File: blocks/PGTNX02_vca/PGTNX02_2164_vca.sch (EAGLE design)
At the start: 72 parts, among them IC3 TL074P

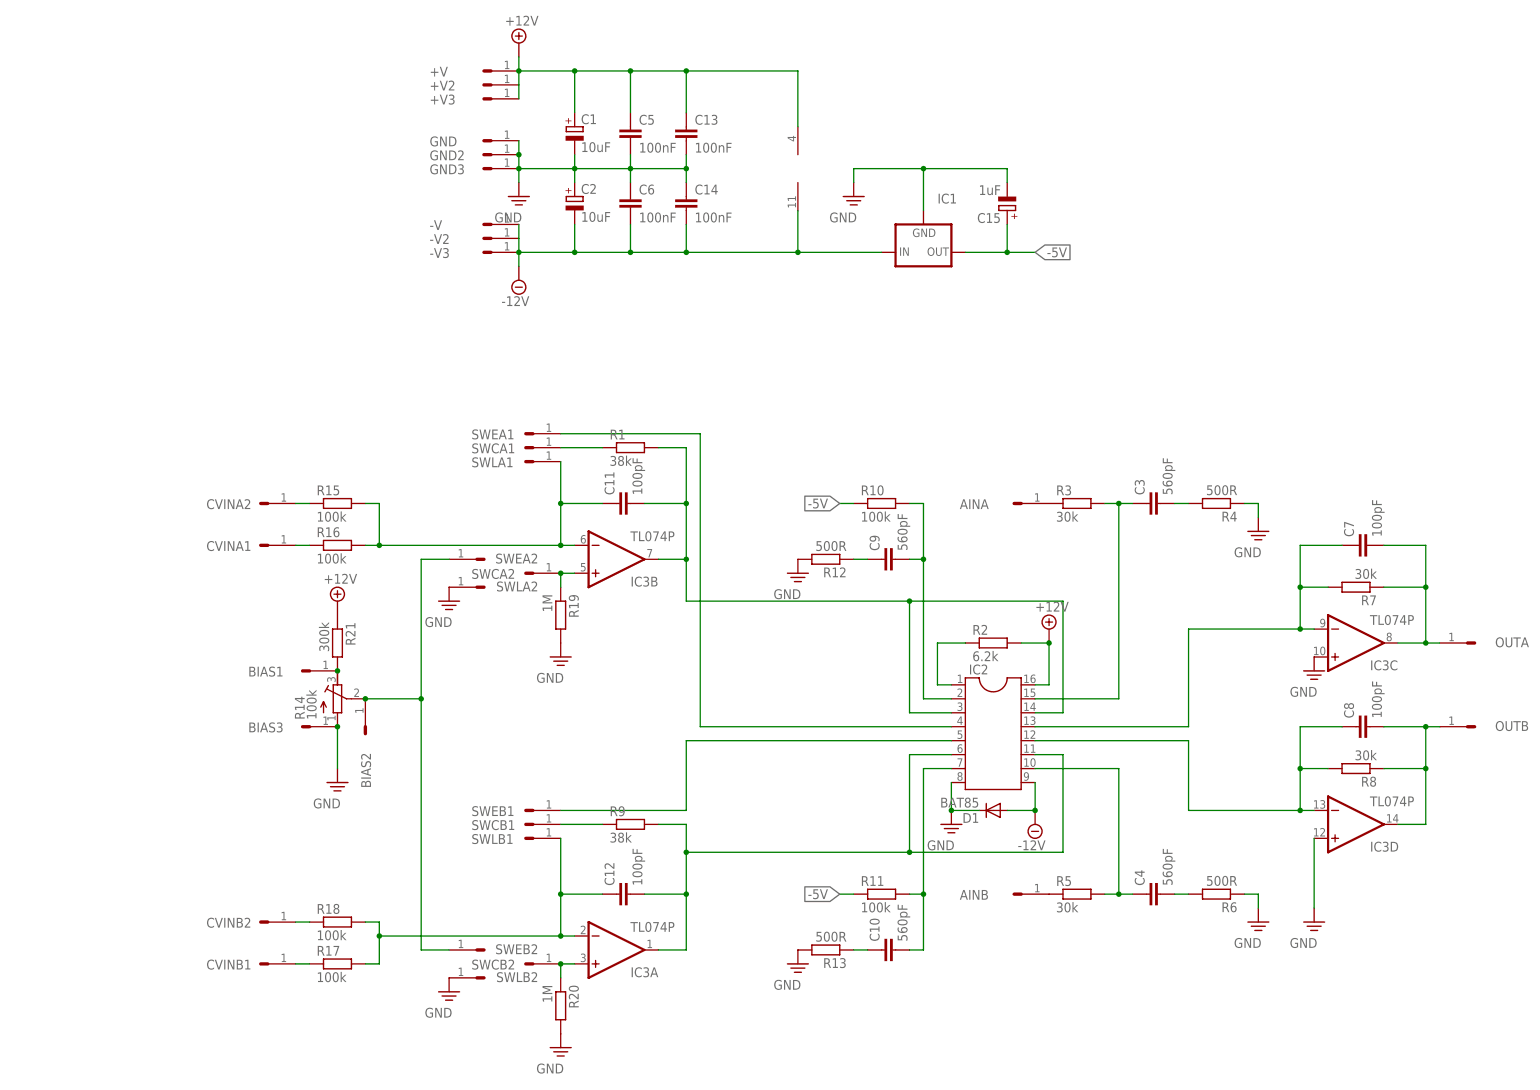
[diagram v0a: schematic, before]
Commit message: 2164 vca board layout + rotary encoder breakout pcb
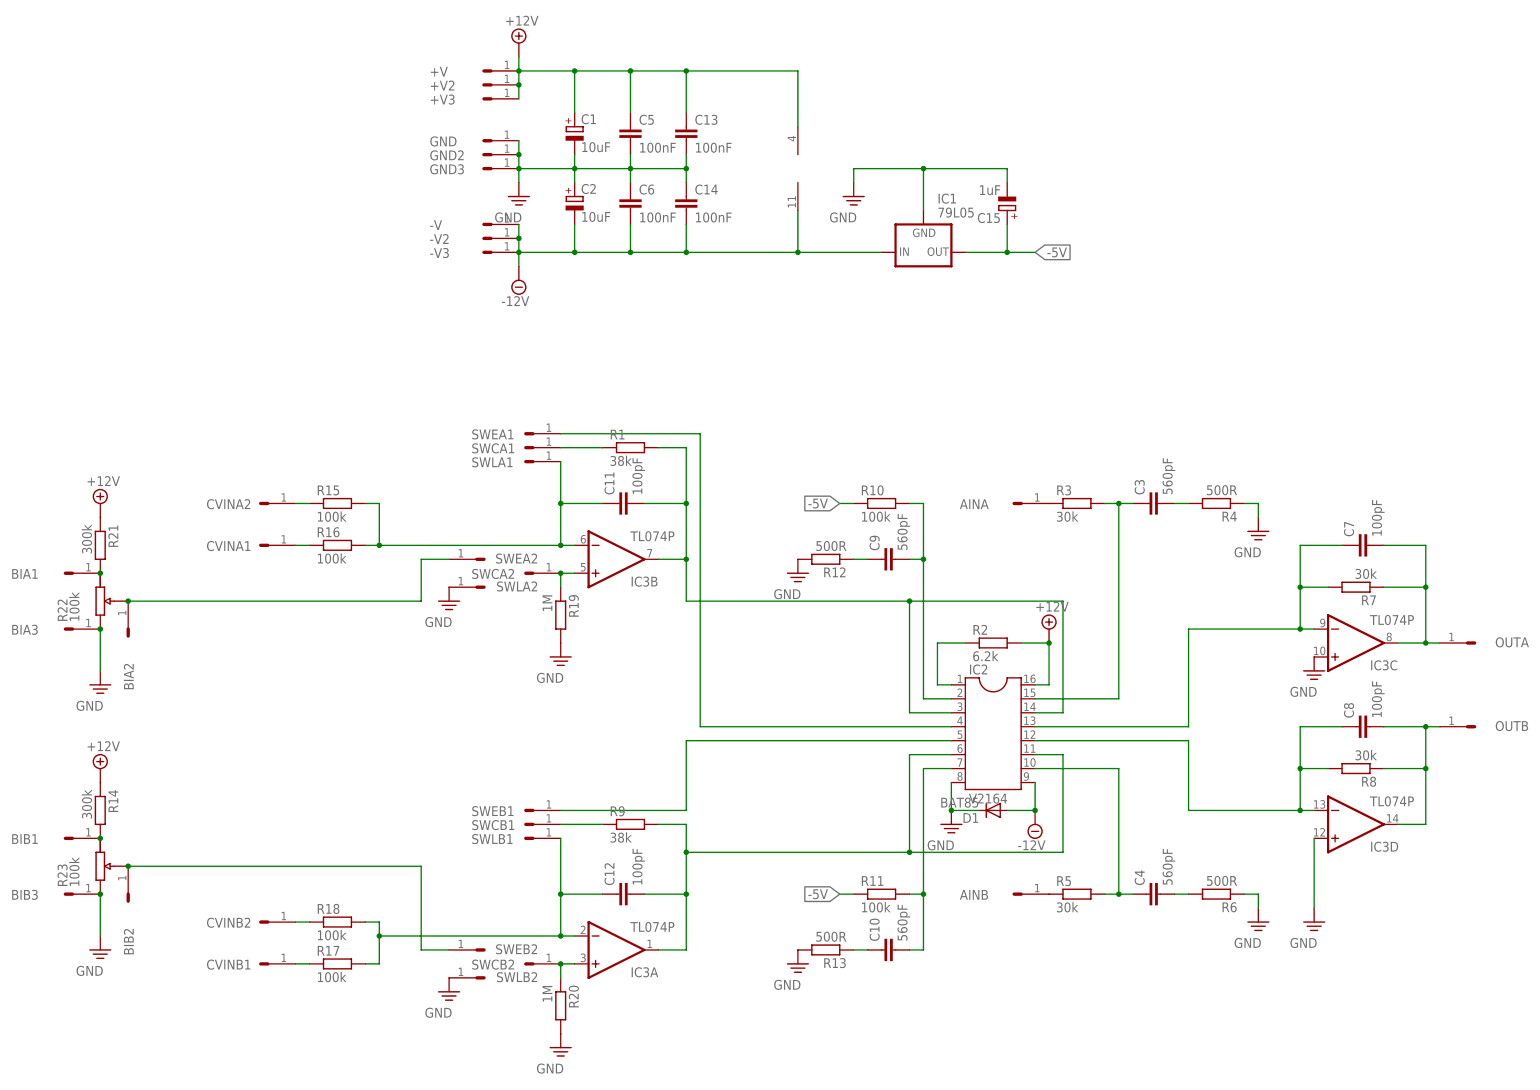
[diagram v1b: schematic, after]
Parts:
- removed BIAS1, BIAS2, BIAS3: HEADER/MALE/01, connectors:HEADER/MALE/01
- added BIA1, BIA2, BIA3, BIB1, BIB2, BIB3: HEADER/MALE/01, connectors:HEADER/MALE/01
- added R22, R23: 100k, controls_off_brd:POTENTIOMETER
- IC1: value (none) -> 79L05
- IC2: value (none) -> V2164
- R14: value 100k -> 300k; device resistors:TRIMMER64X -> resistors:RESISTORRESISTOR/UPRIGHT/7.5
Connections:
- new net N$33: BIB1.3, R14.2, R23.A
- new net N$34: BIA2.3, R22.S, SWEA2.3
- net +12V: now also R14.1
- net N$21: now also BIB2.3, R23.S; no longer BIAS2.3, R14.S, SWEA2.3
- net N$31: now also BIA1.3, R22.A; no longer BIAS1.3, R14.A
- net PE: now also BIA3.3, BIB3.3, R22.E, R23.E; no longer BIAS3.3, R14.E
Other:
- moved on the sheet: R21

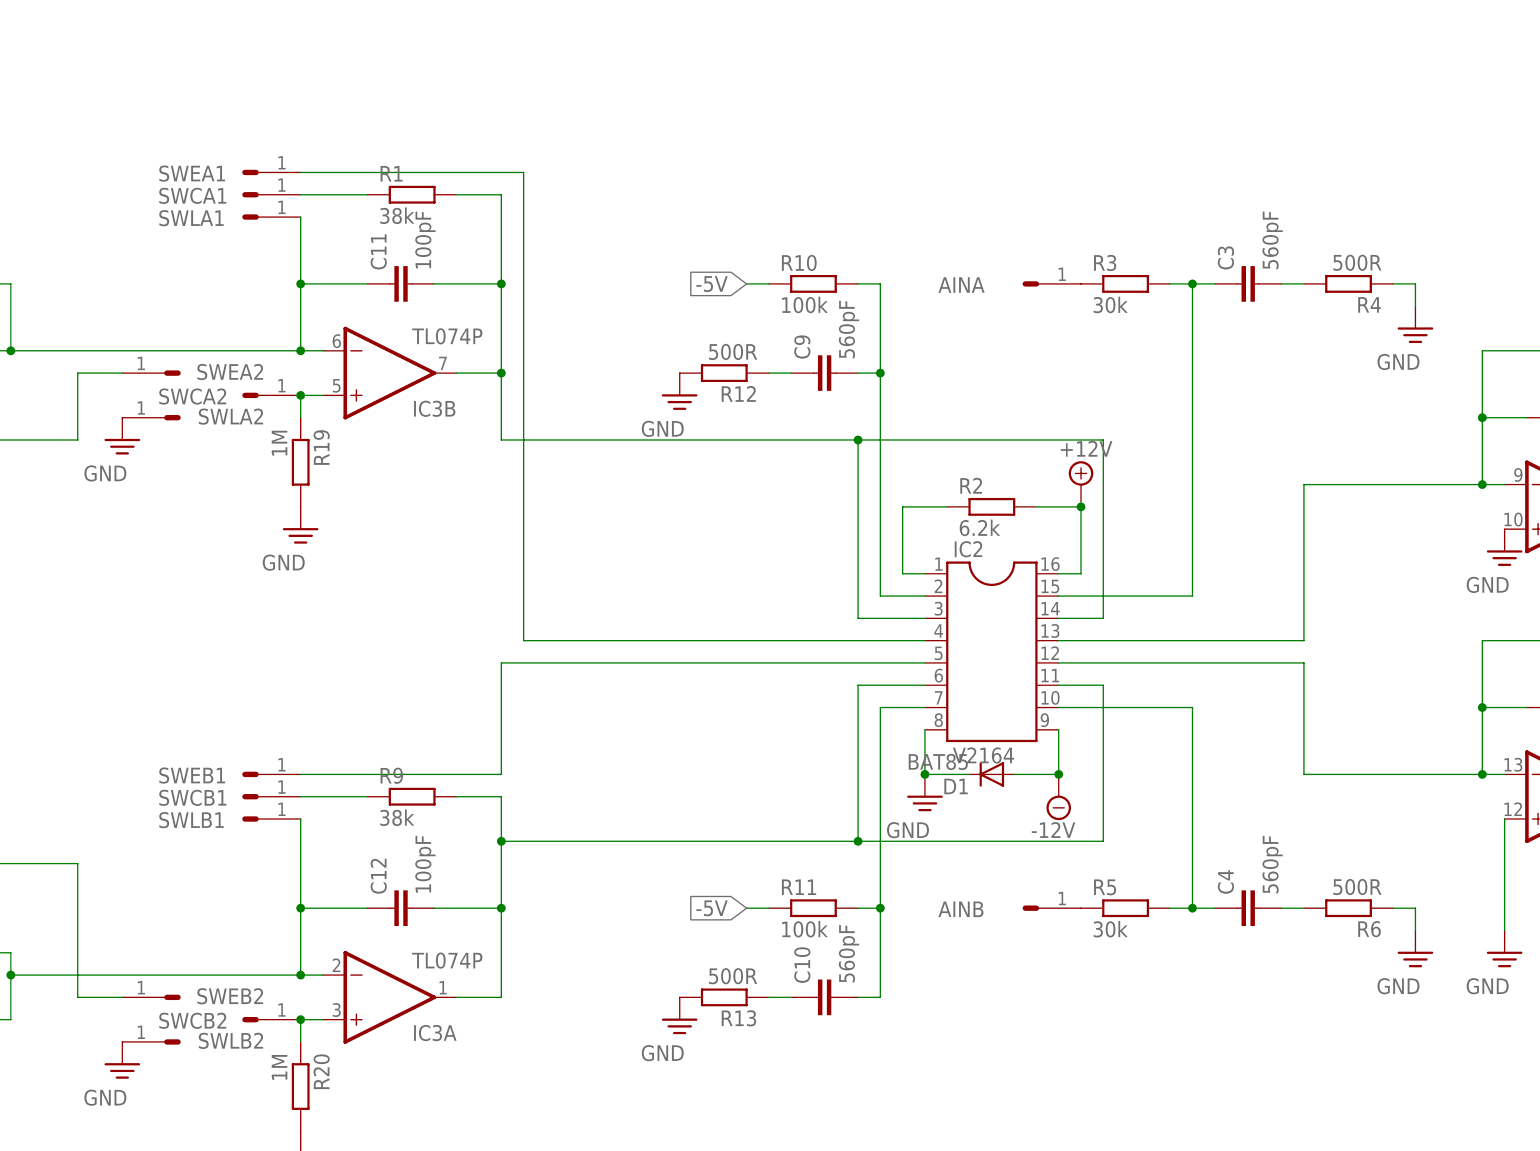
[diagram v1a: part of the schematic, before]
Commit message: Added error history to VCA, corrected some label errors and changed a resistor value.
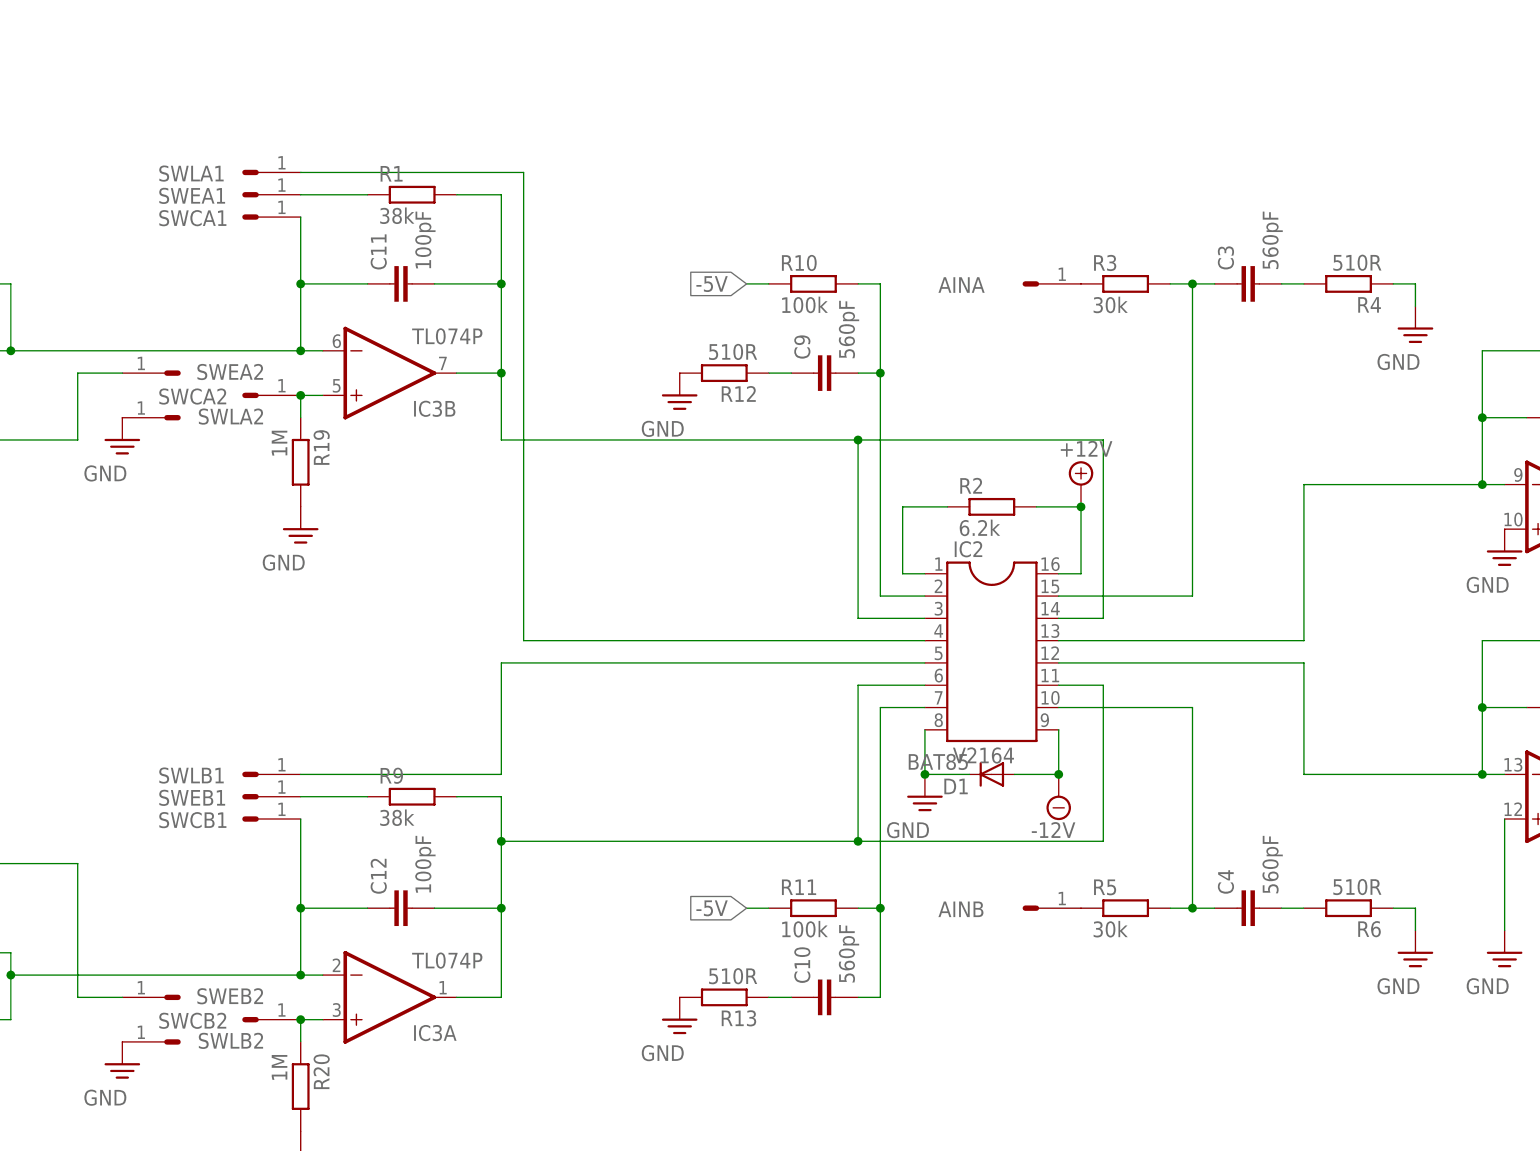
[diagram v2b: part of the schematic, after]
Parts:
- R12, R13, R4, R6: value 500R -> 510R
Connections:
- net N$15: now also SWEA1.3; no longer SWCA1.3
- net N$16: now also SWCA1.3; no longer SWLA1.3
- net N$19: now also SWLA1.3; no longer SWEA1.3
- net N$26: now also SWCB1.3; no longer SWLB1.3
- net N$27: now also SWEB1.3; no longer SWCB1.3
- net N$28: now also SWLB1.3; no longer SWEB1.3
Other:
- moved on the sheet: SWCA1, SWCB1, SWEA1, SWEB1, SWLA1, SWLB1
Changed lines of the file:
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@@
 <part name="R3" library="resistors" deviceset="RESISTOR" device="RESISTOR/UPRIGHT/7.5" value="30k"/>
 <part name="C3" library="capacitors" deviceset="CAPACITOR" device="CERAMICDISC/5" value="560pF"/>
-<part name="R4" library="resistors" deviceset="RESISTOR" device="RESISTOR/UPRIGHT/7.5" value="500R"/>
+<part name="R4" library="resistors" deviceset="RESISTOR" device="RESISTOR/UPRIGHT/7.5" value="510R"/>
 <part name="SUPPLY5" library="supply" deviceset="-12V" device="">
 <attribute name="SPICEPREFIX" value="G"/>
@@
 <part name="R5" library="resistors" deviceset="RESISTOR" device="RESISTOR/UPRIGHT/7.5" value="30k"/>
 <part name="C4" library="capacitors" deviceset="CAPACITOR" device="CERAMICDISC/5" value="560pF"/>
-<part name="R6" library="resistors" deviceset="RESISTOR" device="RESISTOR/UPRIGHT/7.5" value="500R"/>
+<part name="R6" library="resistors" deviceset="RESISTOR" device="RESISTOR/UPRIGHT/7.5" value="510R"/>
 <part name="SUPPLY7" library="supply" deviceset="GND" device="">
 <attribute name="SPICEPREFIX" value="G"/>
@@
 <part name="R11" library="resistors" deviceset="RESISTOR" device="RESISTOR/UPRIGHT/7.5" value="100k"/>
 <part name="C9" library="capacitors" deviceset="CAPACITOR" device="CERAMICDISC/5" value="560pF"/>
-<part name="R12" library="resistors" deviceset="RESISTOR" device="RESISTOR/UPRIGHT/7.5" value="500R"/>
+<part name="R12" library="resistors" deviceset="RESISTOR" device="RESISTOR/UPRIGHT/7.5" value="510R"/>
 <part name="C10" library="capacitors" deviceset="CAPACITOR" device="CERAMICDISC/5" value="560pF"/>
-<part name="R13" library="resistors" deviceset="RESISTOR" device="RESISTOR/UPRIGHT/7.5" value="500R"/>
+<part name="R13" library="resistors" deviceset="RESISTOR" device="RESISTOR/UPRIGHT/7.5" value="510R"/>
 <part name="C11" library="capacitors" deviceset="CAPACITOR" device="CERAMICDISC/5" value="100pF"/>
 <part name="C12" library="capacitors" deviceset="CAPACITOR" device="CERAMICDISC/5" value="100pF"/>
@@
 <part name="C13" library="capacitors" deviceset="CAPACITOR" device="CERAMICDISC/5" value="100nF"/>
 <part name="C14" library="capacitors" deviceset="CAPACITOR" device="CERAMICDISC/5" value="100nF"/>
-<part name="SWLA1" library="connectors" deviceset="HEADER/MALE/01" device=""/>
 <part name="SWCA1" library="connectors" deviceset="HEADER/MALE/01" device=""/>
 <part name="SWEA1" library="connectors" deviceset="HEADER/MALE/01" device=""/>
-<part name="SWLB1" library="connectors" deviceset="HEADER/MALE/01" device=""/>
+<part name="SWLA1" library="connectors" deviceset="HEADER/MALE/01" device=""/>
 <part name="SWCB1" library="connectors" deviceset="HEADER/MALE/01" device=""/>
 <part name="SWEB1" library="connectors" deviceset="HEADER/MALE/01" device=""/>
+<part name="SWLB1" library="connectors" deviceset="HEADER/MALE/01" device=""/>
 <part name="R19" library="resistors" deviceset="RESISTOR" device="RESISTOR/UPRIGHT/7.5" value="1M"/>
 <part name="R20" library="resistors" deviceset="RESISTOR" device="RESISTOR/UPRIGHT/7.5" value="1M"/>
@@
 <attribute name="VALUE" x="54.864" y="68.961" size="1.778" layer="96"/>
 </instance>
-<instance part="SWLA1" gate="HEADER" x="27.94" y="25.4" smashed="yes">
+<instance part="SWCA1" gate="HEADER" x="27.94" y="25.4" smashed="yes">
 <attribute name="NAME" x="14.224" y="24.384" size="1.778" layer="96"/>
 </instance>
-<instance part="SWCA1" gate="HEADER" x="27.94" y="27.94" smashed="yes">
+<instance part="SWEA1" gate="HEADER" x="27.94" y="27.94" smashed="yes">
 <attribute name="NAME" x="14.224" y="26.924" size="1.778" layer="96"/>
 </instance>
-<instance part="SWEA1" gate="HEADER" x="27.94" y="30.48" smashed="yes">
+<instance part="SWLA1" gate="HEADER" x="27.94" y="30.48" smashed="yes">
 <attribute name="NAME" x="14.224" y="29.464" size="1.778" layer="96"/>
 </instance>
-<instance part="SWLB1" gate="HEADER" x="27.94" y="-43.18" smashed="yes">
+<instance part="SWCB1" gate="HEADER" x="27.94" y="-43.18" smashed="yes">
 <attribute name="NAME" x="14.224" y="-44.196" size="1.778" layer="96"/>
 </instance>
-<instance part="SWCB1" gate="HEADER" x="27.94" y="-40.64" smashed="yes">
+<instance part="SWEB1" gate="HEADER" x="27.94" y="-40.64" smashed="yes">
 <attribute name="NAME" x="14.224" y="-41.656" size="1.778" layer="96"/>
 </instance>
-<instance part="SWEB1" gate="HEADER" x="27.94" y="-38.1" smashed="yes">
+<instance part="SWLB1" gate="HEADER" x="27.94" y="-38.1" smashed="yes">
 <attribute name="NAME" x="14.224" y="-39.116" size="1.778" layer="96"/>
 </instance>
@@
 <wire x1="-2.54" y1="-58.42" x2="-2.54" y2="-60.96" width="0.1524" layer="91"/>
 <junction x="-2.54" y="-60.96"/>
-<pinref part="SWLB1" gate="HEADER" pin="3"/>
+<pinref part="SWCB1" gate="HEADER" pin="3"/>
 <wire x1="30.48" y1="-53.34" x2="30.48" y2="-43.18" width="0.1524" layer="91"/>
 <junction x="30.48" y="-53.34"/>
@@
 <segment>
 <pinref part="R1" gate="G$1" pin="1"/>
+<pinref part="SWEA1" gate="HEADER" pin="3"/>
+<wire x1="30.48" y1="27.94" x2="38.1" y2="27.94" width="0.1524" layer="91"/>
+</segment>
+</net>
+<net name="N$16" class="0">
+<segment>
+<pinref part="C11" gate="G$1" pin="1"/>
 <pinref part="SWCA1" gate="HEADER" pin="3"/>
-<wire x1="30.48" y1="27.94" x2="38.1" y2="27.94" width="0.1524" layer="91"/>
-</segment>
-</net>
-<net name="N$16" class="0">
-<segment>
-<pinref part="C11" gate="G$1" pin="1"/>
-<pinref part="SWLA1" gate="HEADER" pin="3"/>
 <wire x1="38.1" y1="17.78" x2="30.48" y2="17.78" width="0.1524" layer="91"/>
 <wire x1="30.48" y1="17.78" x2="30.48" y2="25.4" width="0.1524" layer="91"/>
@@
 <wire x1="101.6" y1="-22.86" x2="55.88" y2="-22.86" width="0.1524" layer="91"/>
 <wire x1="55.88" y1="-22.86" x2="55.88" y2="30.48" width="0.1524" layer="91"/>
-<pinref part="SWEA1" gate="HEADER" pin="3"/>
+<pinref part="SWLA1" gate="HEADER" pin="3"/>
 <wire x1="55.88" y1="30.48" x2="30.48" y2="30.48" width="0.1524" layer="91"/>
 </segment>
@@
 <segment>
 <pinref part="R9" gate="G$1" pin="1"/>
-<pinref part="SWCB1" gate="HEADER" pin="3"/>
+<pinref part="SWEB1" gate="HEADER" pin="3"/>
 <wire x1="38.1" y1="-40.64" x2="30.48" y2="-40.64" width="0.1524" layer="91"/>
 </segment>
@@
 <net name="N$28" class="0">
 <segment>
-<pinref part="SWEB1" gate="HEADER" pin="3"/>
+<pinref part="SWLB1" gate="HEADER" pin="3"/>
 <wire x1="30.48" y1="-38.1" x2="53.34" y2="-38.1" width="0.1524" layer="91"/>
 <wire x1="53.34" y1="-38.1" x2="53.34" y2="-25.4" width="0.1524" layer="91"/>
